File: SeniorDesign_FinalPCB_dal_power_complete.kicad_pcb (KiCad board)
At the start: 2 copper layers, 172.7 x 167.4 mm, 226 parts, among them J1 5000, J10 5000, J11 POWER, J2 5000, J3 5000, J4 5000, J5 5000, J6 5000, J7 5000, J8 5000, J9 5000, Q1 Si7450DP, Q10 Si7450DP, Q11 Si7450DP, Q12 Si7450DP, Q13 Si7450DP, Q14 Si7450DP, Q15 Si7450DP, Q16 Si7450DP, Q2 Si7450DP, Q3 Si7450DP, Q4 Si7450DP, Q5 Si7450DP, Q6 Si7450DP, Q7 Si7450DP, Q8 Si7450DP, Q9 Si7450DP, U1 Transducer, U10 Transducer, U11 Transducer, U12 Transducer, U13 Transducer, U14 Transducer, U15 Transducer, U16 Transducer, U17 Transducer, U18 Transducer, U19 Transducer, U2 Transducer, U20 Transducer, U21 Transducer, U22 Transducer, U23 Transducer, U24 Transducer, U25 Transducer, U26 Transducer, U27 Transducer, U28 Transducer, U29 Transducer, U3 Transducer, U30 Transducer, U31 Transducer, U32 Transducer, U33 Transducer, U34 Transducer, U35 Transducer, U36 Transducer, U37 Transducer, U38 Transducer, U39 Transducer, U4 Transducer, U40 Transducer, U41 Transducer, U42 Transducer, U43 Transducer, U44 Transducer, U45 Transducer, U46 Transducer, U47 Transducer, U48 Transducer, U49 Transducer, U5 Transducer, U50 Transducer, U51 Transducer, U52 Transducer, U53 Transducer, U54 Transducer, U55 Transducer, U56 Transducer, U57 Transducer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

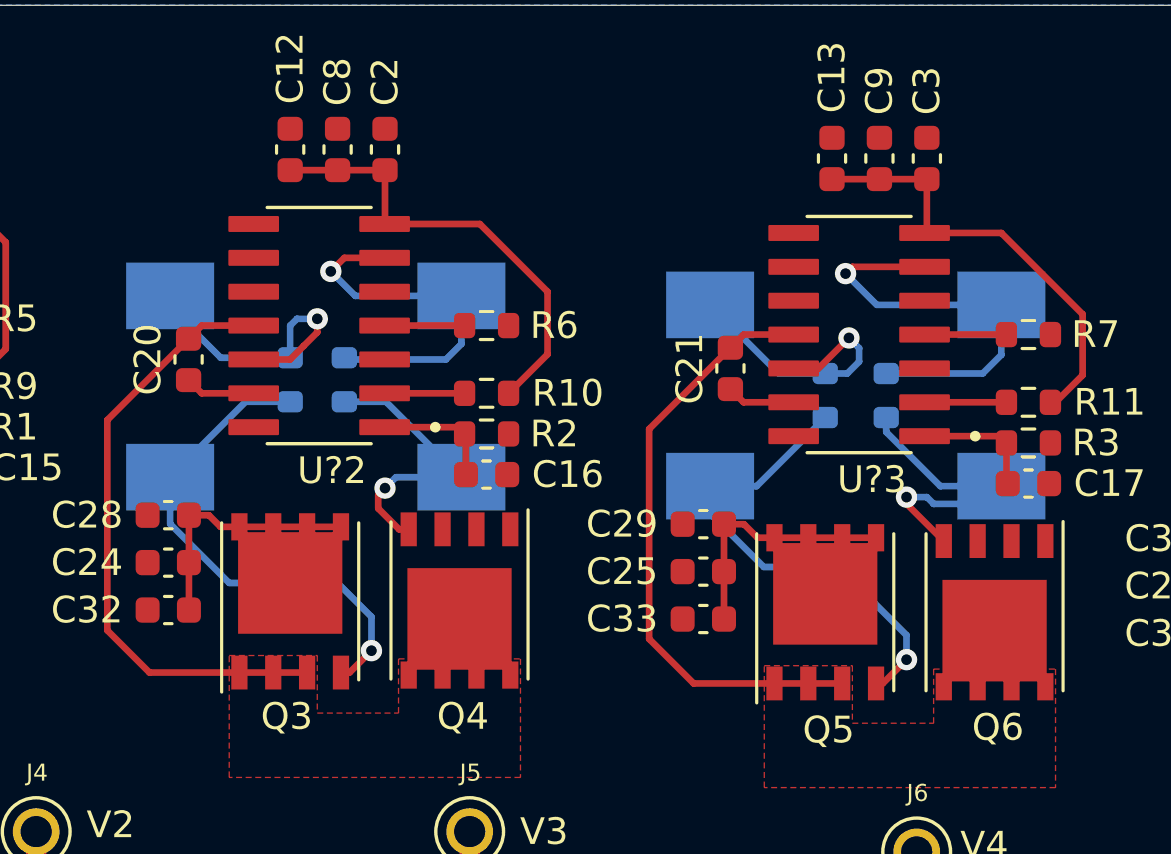
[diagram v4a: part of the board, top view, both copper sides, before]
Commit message: channel 2 and 3 trace widths
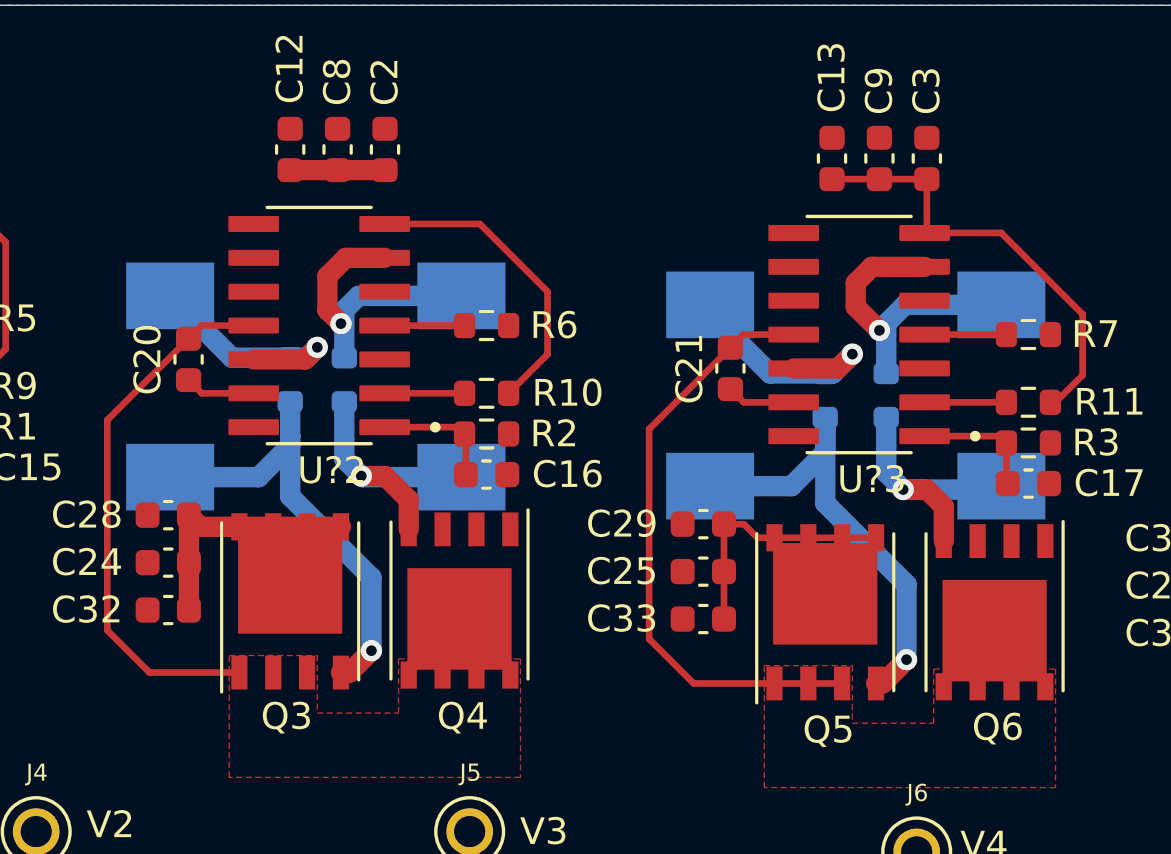
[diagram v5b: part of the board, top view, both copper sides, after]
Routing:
- net Net-(D6-Pad1): track 15.9 -> 11.3 mm
- net Net-(D4-Pad1): track 14.0 -> 10.8 mm
- net /pwm_driver/COL2_OUT: track 23.3 -> 20.8 mm
- net +12V: track 141.1 -> 139.1 mm
- net Net-(D3-Pad1): track 11.4 -> 9.71 mm
- net Net-(D3-Pad2): track 19.2 -> 17.5 mm
- net Net-(D6-Pad2): track 11.9 -> 10.7 mm
- net Net-(D5-Pad1): track 10.4 -> 9.31 mm
- net Net-(D4-Pad2): track 10.9 -> 10.1 mm
- net Net-(D5-Pad2): track 18.1 -> 18.6 mm

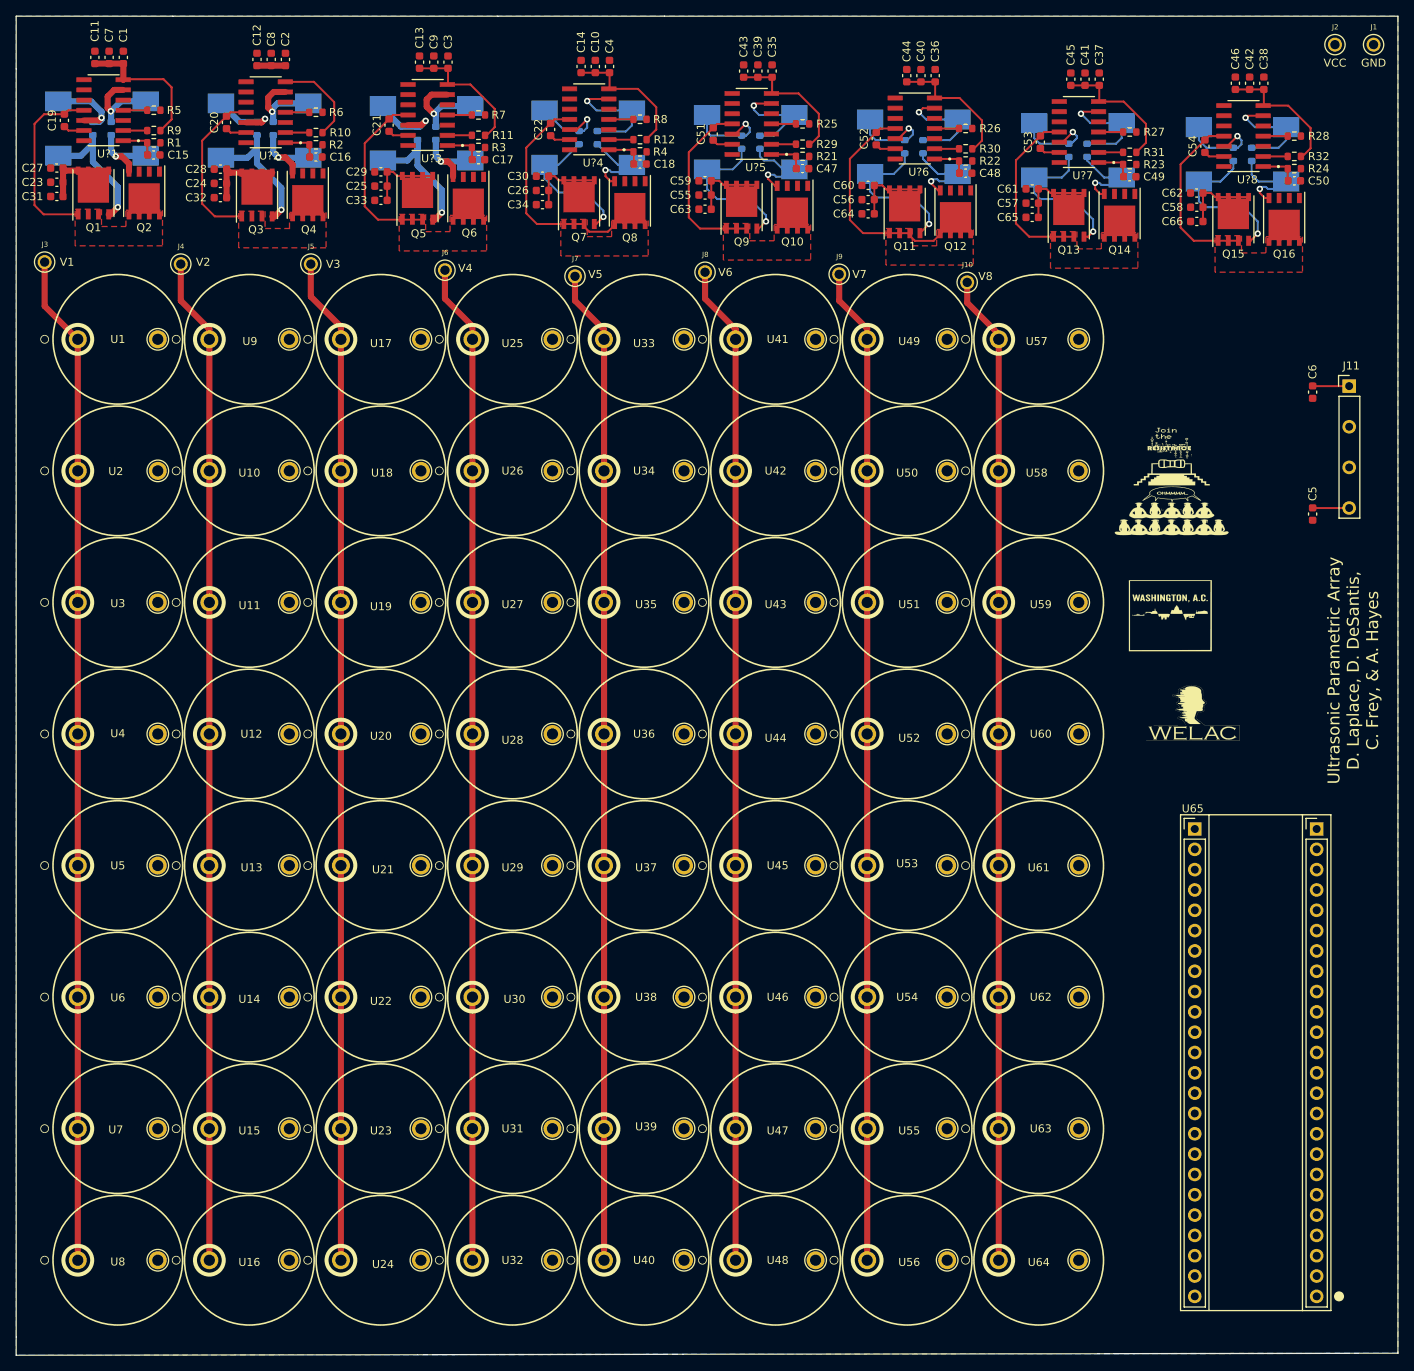
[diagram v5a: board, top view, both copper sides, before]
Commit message: Finished trace widths on channels 4-8
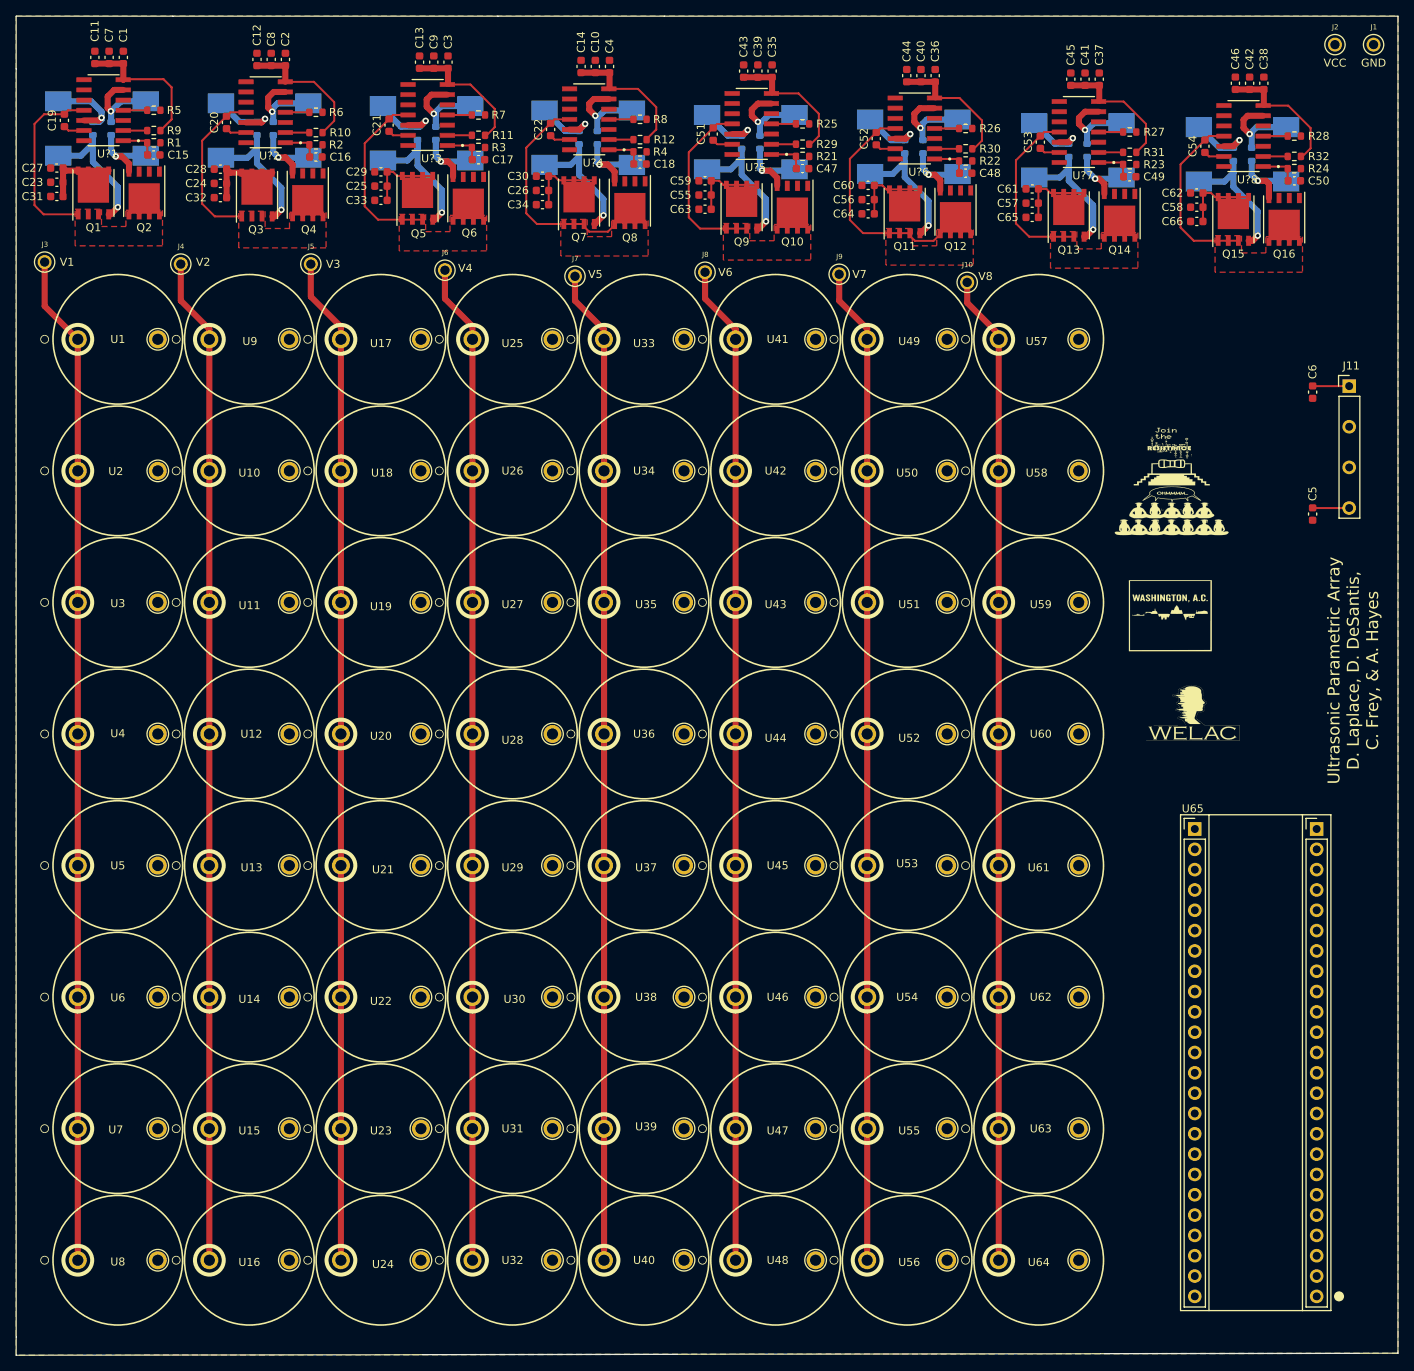
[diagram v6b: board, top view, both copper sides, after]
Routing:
- net Net-(D8-Pad1): track 15.4 -> 10.9 mm
- net Net-(D14-Pad1): track 14.4 -> 11.0 mm
- net Net-(D13-Pad2): track 20.0 -> 16.6 mm
- net Net-(D9-Pad1): track 11.8 -> 8.59 mm
- net Net-(D15-Pad2): track 19.8 -> 16.8 mm
- net Net-(D11-Pad2): track 19.7 -> 16.7 mm
- net Net-(D9-Pad2): track 19.7 -> 16.7 mm
- net Net-(D16-Pad1): track 14.2 -> 11.3 mm
- net Net-(D13-Pad1): track 11.0 -> 8.20 mm
- net Net-(D10-Pad1): track 13.6 -> 10.9 mm
- net Net-(D11-Pad1): track 11.1 -> 8.56 mm
- net Net-(D16-Pad2): track 12.2 -> 9.72 mm
- net Net-(D14-Pad2): track 11.6 -> 9.19 mm
- net Net-(D12-Pad1): track 13.7 -> 11.6 mm
- net Net-(D15-Pad1): track 11.0 -> 8.92 mm
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- added copper zone on F.Cu, net GND

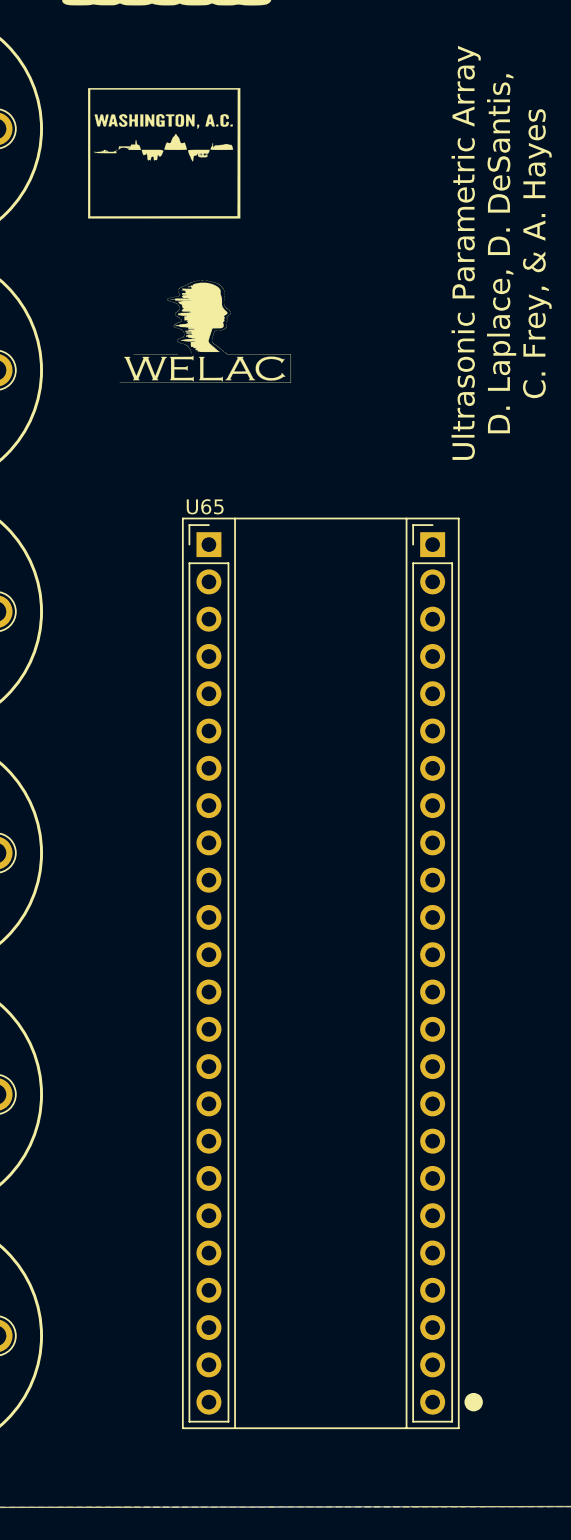
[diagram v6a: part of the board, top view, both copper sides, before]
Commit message: Rotate CMOD on pcb so usb points towards the edge.
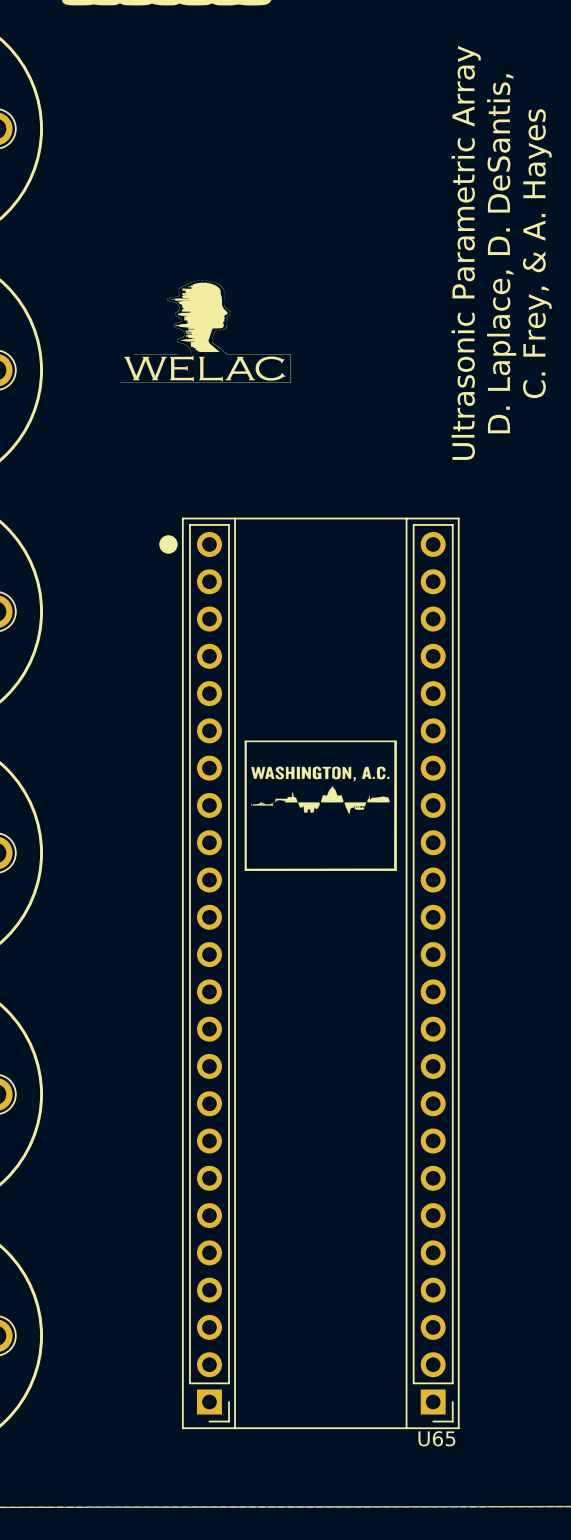
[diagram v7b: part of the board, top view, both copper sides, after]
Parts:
- moved U65 60.4 mm to (449.6, 179.8), turned to 180 degrees
- moved G*** 45.7 mm to (457.2, 139.2)
